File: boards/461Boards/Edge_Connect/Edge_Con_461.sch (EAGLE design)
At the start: 8 parts, among them IC1 TINY26P

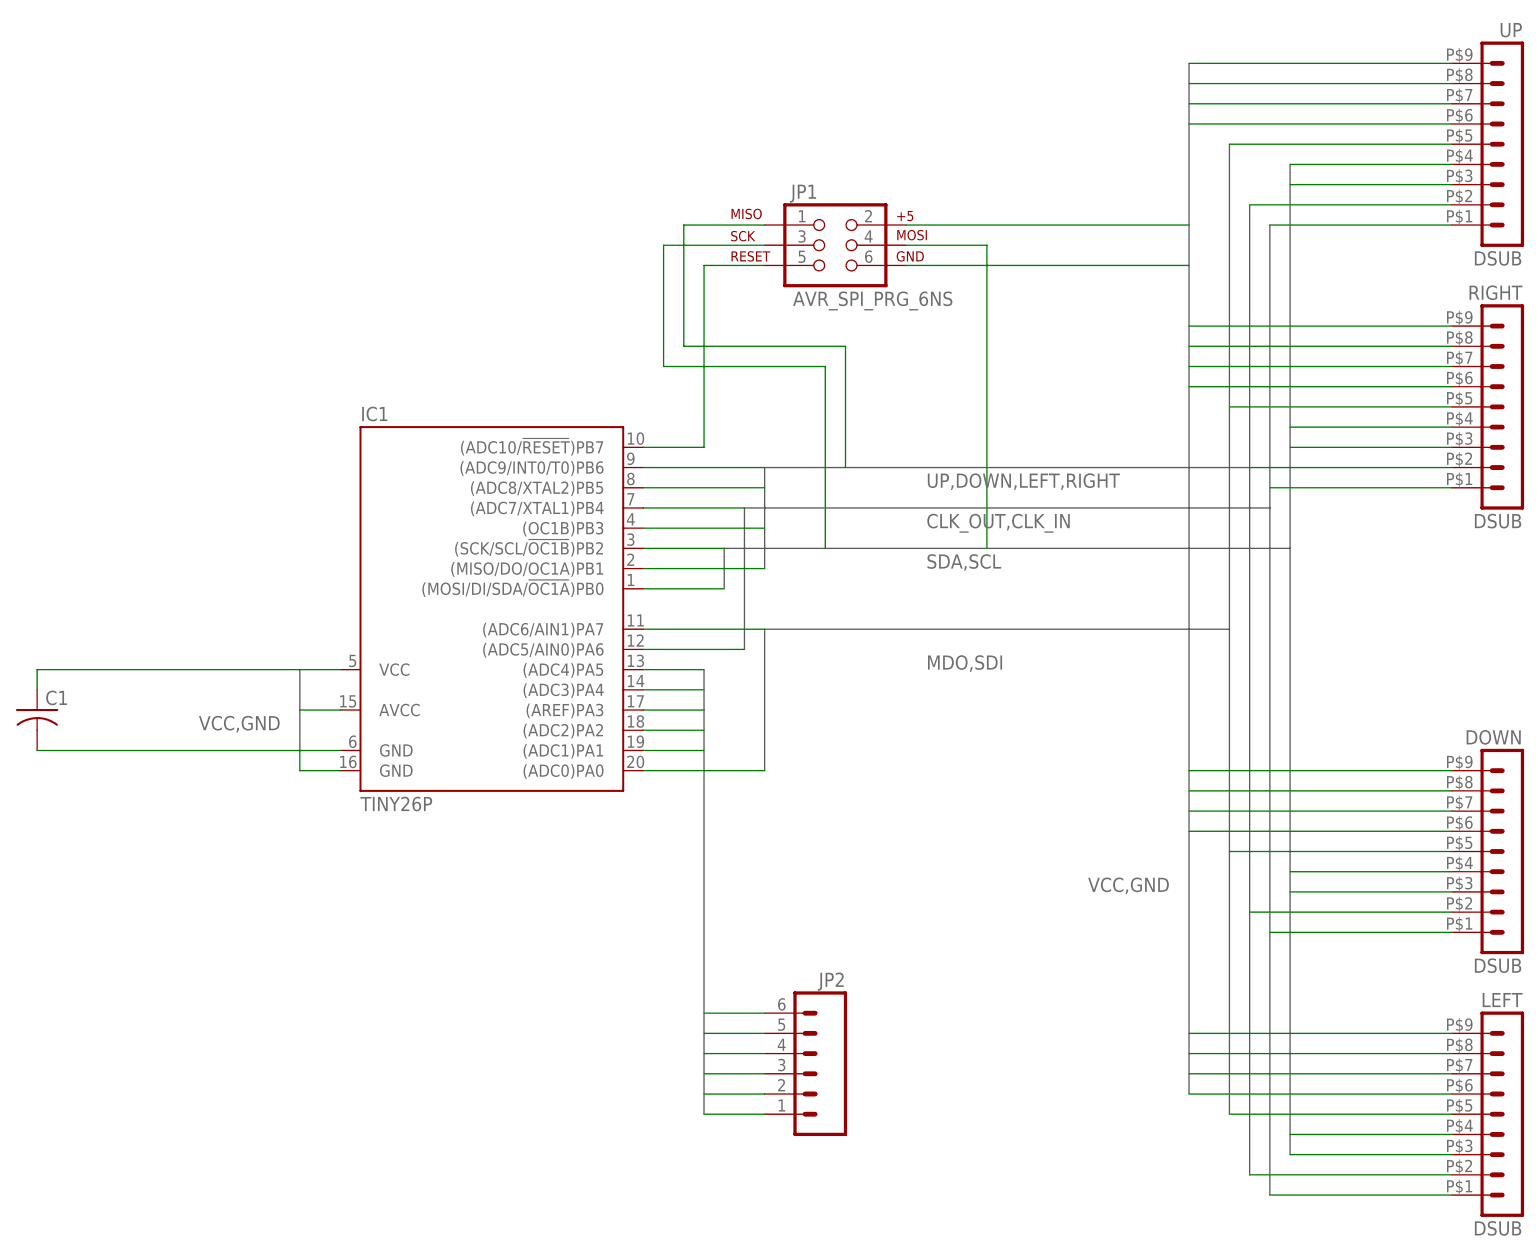
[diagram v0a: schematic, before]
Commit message: Layout in progress, one footprint needs to be added to 461_Edge Connect prior to cut.
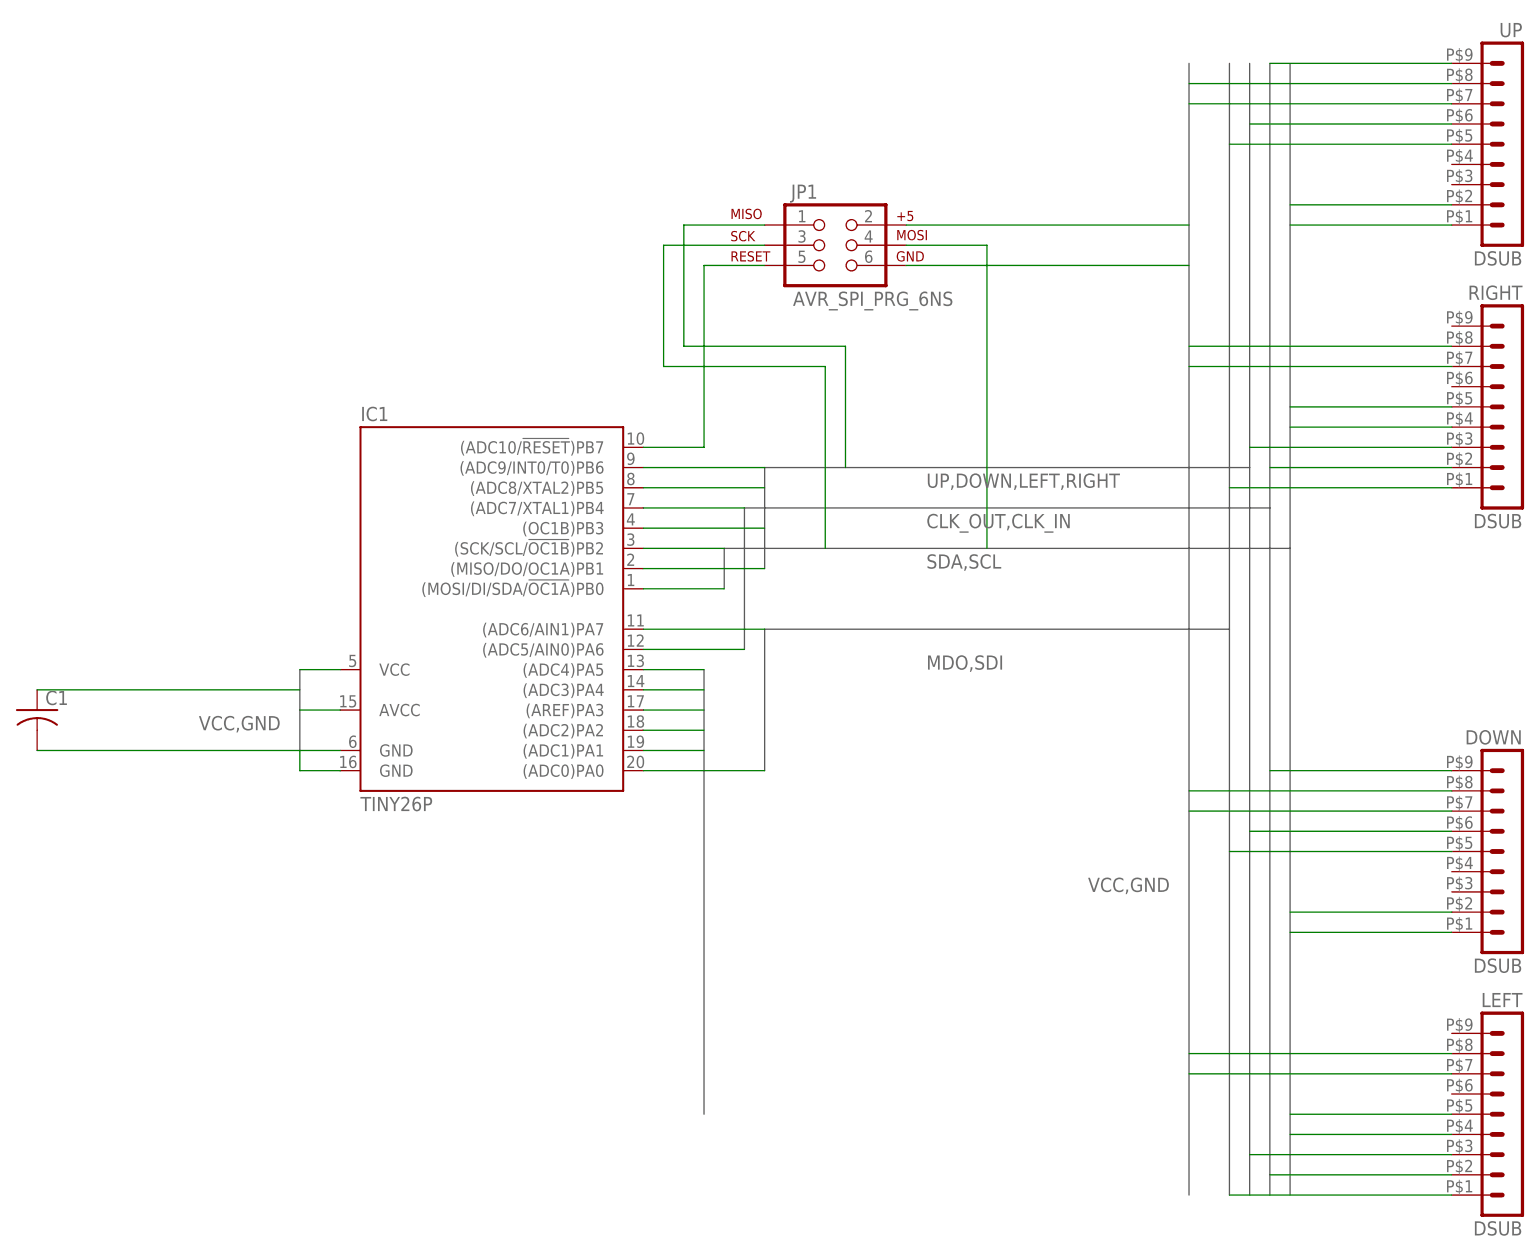
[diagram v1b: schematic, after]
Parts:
- removed JP2: (no value), SparkFun-Connectors:M06SILK_FEMALE_PTH
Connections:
- removed net 16: JP2.3
- net 13: no longer JP2.1
- net 14: no longer JP2.2
- net 17: no longer JP2.4
- net 18: no longer JP2.5
- net 19: no longer JP2.6
- net CLK_IN: now also DOWN.9, LEFT.2; no longer DOWN.1, LEFT.1
- net CLK_OUT: now also RIGHT.2, UP.9; no longer RIGHT.1, UP.1
- net DOWN: now also DOWN.6; no longer DOWN.2
- net GND: no longer DOWN.8, LEFT.8, RIGHT.8, UP.8
- net LEFT: now also LEFT.3; no longer LEFT.2
- net MDO: now also RIGHT.1; no longer RIGHT.5
- net RIGHT: now also RIGHT.3; no longer RIGHT.2
- net SCL: now also DOWN.2, LEFT.5, RIGHT.5, UP.2; no longer DOWN.4, LEFT.4, RIGHT.4, UP.4
- net SDA: now also DOWN.1, LEFT.4, RIGHT.4, UP.1; no longer DOWN.3, LEFT.3, RIGHT.3, UP.3
- net SDI: now also LEFT.1; no longer LEFT.5
- net UP: now also UP.6; no longer UP.2
- net VCC: now also DOWN.8, LEFT.8, RIGHT.8, UP.8; no longer DOWN.6, DOWN.9, LEFT.6, LEFT.9, RIGHT.6, RIGHT.9, UP.6, UP.9

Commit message: Edge Connect Layout Complete V1.0, 3 Jumper Function Select, 2 LED spaces available, Push Button Reset.
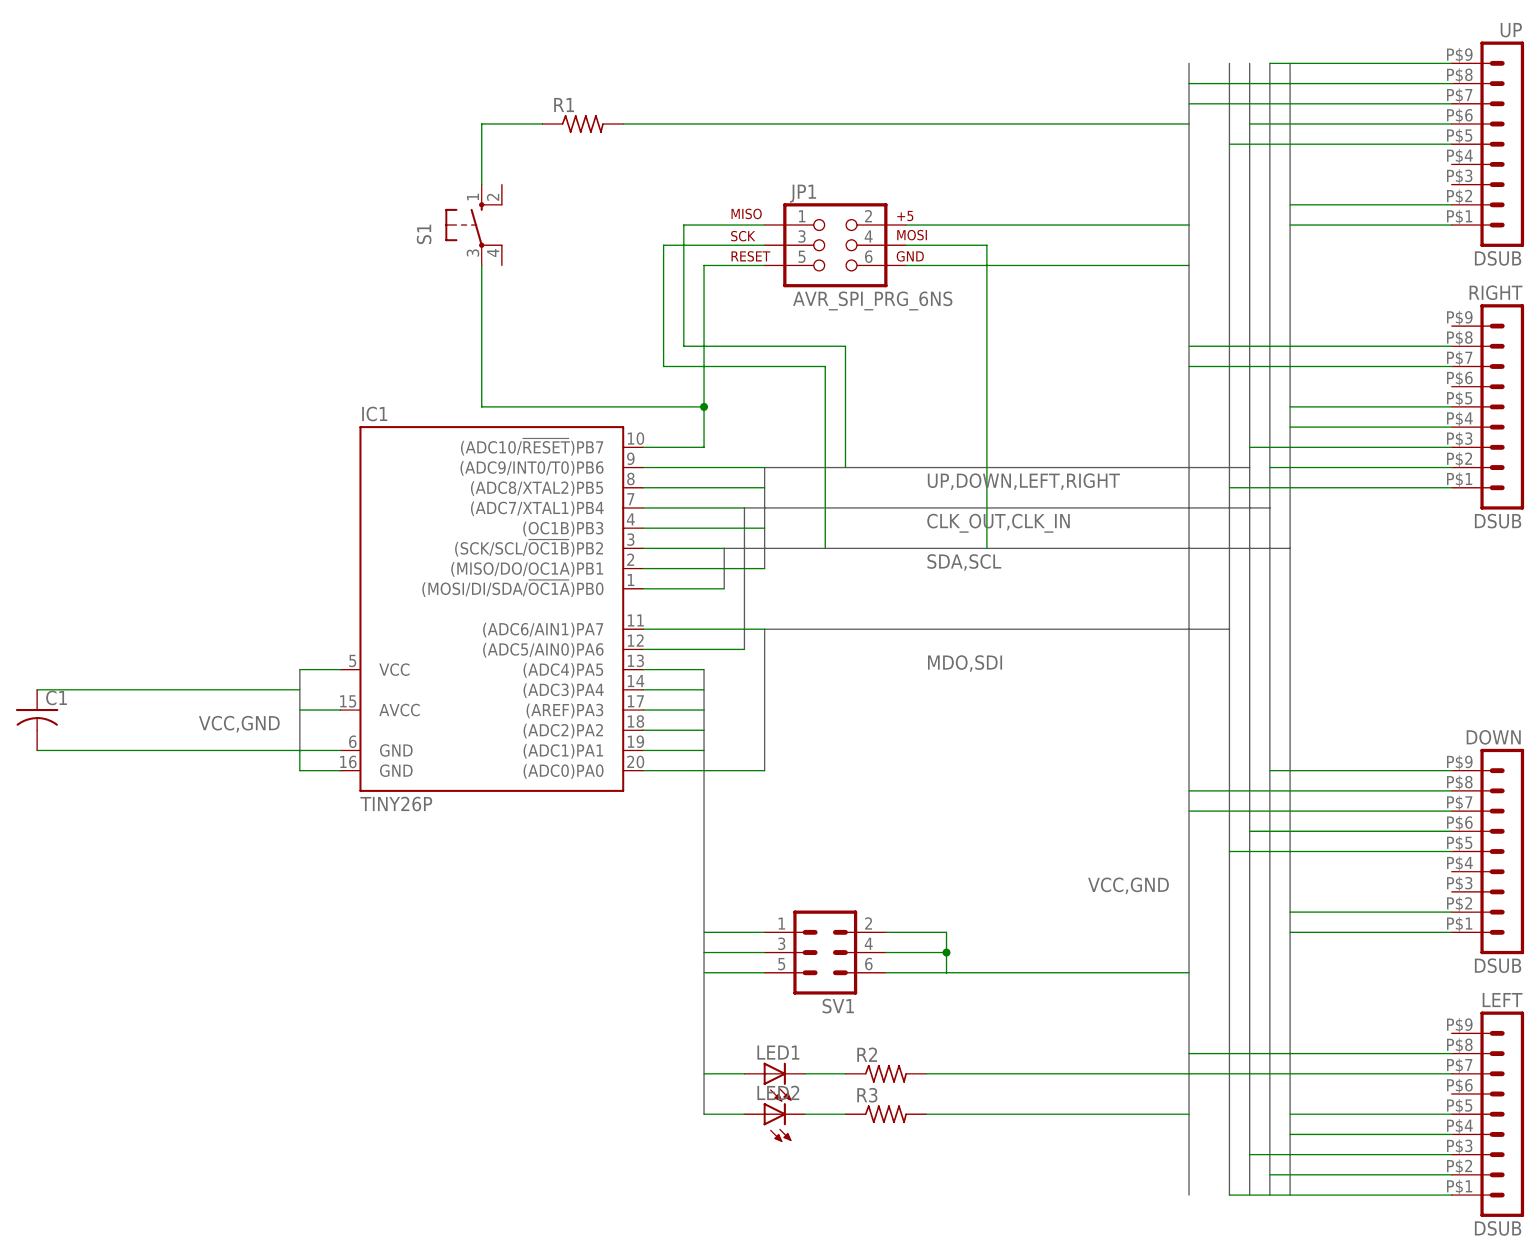
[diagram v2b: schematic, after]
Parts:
- added LED1, LED2: (no value), led:LED3MM
- added R1, R2, R3: (no value), rcl:R-US_0204/5
- added S1: (no value), switch-omron:10-XX
- added SV1: (no value), con-lstb:MA03-2
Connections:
- new net N$2: R1.1, S1.S
- new net N$3: LED1.C, R2.1
- new net N$4: LED2.C, R3.1
- net 13: now also LED1.A
- net 14: now also LED2.A
- net 17: now also SV1.5
- net 18: now also SV1.3
- net 19: now also SV1.1
- net GND: now also R1.2, R2.2, R3.2, SV1.2, SV1.4, SV1.6
- net N$1: now also S1.P
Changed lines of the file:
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@@
 <part name="JP1" library="SparkFun-Connectors" deviceset="AVR_SPI_PRG_6" device="NS"/>
 <part name="C1" library="rcl" deviceset="C-US" device="025-025X050"/>
+<part name="SV1" library="con-lstb" deviceset="MA03-2" device=""/>
+<part name="S1" library="switch-omron" deviceset="10-XX" device=""/>
+<part name="R1" library="rcl" deviceset="R-US_" device="0204/5"/>
+<part name="R2" library="rcl" deviceset="R-US_" device="0204/5"/>
+<part name="R3" library="rcl" deviceset="R-US_" device="0204/5"/>
+<part name="LED1" library="led" deviceset="LED" device="3MM"/>
+<part name="LED2" library="led" deviceset="LED" device="3MM"/>
 </parts>
 <sheets>
@@
 <instance part="JP1" gate="G$1" x="-33.02" y="53.34"/>
 <instance part="C1" gate="G$1" x="-132.08" y="-5.08"/>
+<instance part="SV1" gate="1" x="-33.02" y="-35.56" rot="R180"/>
+<instance part="S1" gate="1" x="-76.2" y="55.88"/>
+<instance part="R1" gate="G$1" x="-63.5" y="68.58"/>
+<instance part="R2" gate="G$1" x="-25.4" y="-50.8"/>
+<instance part="R3" gate="G$1" x="-25.4" y="-55.88"/>
+<instance part="LED1" gate="G$1" x="-40.64" y="-50.8" rot="R90"/>
+<instance part="LED2" gate="G$1" x="-40.64" y="-55.88" rot="R90"/>
 </instances>
 <busses>
@@
 <wire x1="-132.08" y1="-10.16" x2="-99.06" y2="-10.16" width="0.1524" layer="91"/>
 </segment>
+<segment>
+<pinref part="SV1" gate="1" pin="2"/>
+<wire x1="-25.4" y1="-33.02" x2="-17.78" y2="-33.02" width="0.1524" layer="91"/>
+<pinref part="SV1" gate="1" pin="6"/>
+<wire x1="-17.78" y1="-33.02" x2="-17.78" y2="-35.56" width="0.1524" layer="91"/>
+<wire x1="-17.78" y1="-35.56" x2="-17.78" y2="-38.1" width="0.1524" layer="91"/>
+<wire x1="-17.78" y1="-38.1" x2="-25.4" y2="-38.1" width="0.1524" layer="91"/>
+<pinref part="SV1" gate="1" pin="4"/>
+<wire x1="-25.4" y1="-35.56" x2="-17.78" y2="-35.56" width="0.1524" layer="91"/>
+<junction x="-17.78" y="-35.56"/>
+<wire x1="12.7" y1="-38.1" x2="-17.78" y2="-38.1" width="0.1524" layer="91"/>
+</segment>
+<segment>
+<pinref part="R1" gate="G$1" pin="2"/>
+<wire x1="-58.42" y1="68.58" x2="12.7" y2="68.58" width="0.1524" layer="91"/>
+</segment>
+<segment>
+<pinref part="R2" gate="G$1" pin="2"/>
+<wire x1="-20.32" y1="-50.8" x2="12.7" y2="-50.8" width="0.1524" layer="91"/>
+</segment>
+<segment>
+<pinref part="R3" gate="G$1" pin="2"/>
+<wire x1="-20.32" y1="-55.88" x2="12.7" y2="-55.88" width="0.1524" layer="91"/>
+</segment>
 </net>
 <net name="13" class="0">
@@
 <wire x1="-55.88" y1="0" x2="-48.26" y2="0" width="0.1524" layer="91"/>
 </segment>
+<segment>
+<pinref part="LED1" gate="G$1" pin="A"/>
+<wire x1="-48.26" y1="-50.8" x2="-43.18" y2="-50.8" width="0.1524" layer="91"/>
+</segment>
 </net>
 <net name="14" class="0">
@@
 <wire x1="-55.88" y1="-2.54" x2="-48.26" y2="-2.54" width="0.1524" layer="91"/>
 </segment>
+<segment>
+<pinref part="LED2" gate="G$1" pin="A"/>
+<wire x1="-48.26" y1="-55.88" x2="-43.18" y2="-55.88" width="0.1524" layer="91"/>
+</segment>
 </net>
 <net name="17" class="0">
@@
 <wire x1="-55.88" y1="-5.08" x2="-48.26" y2="-5.08" width="0.1524" layer="91"/>
 </segment>
+<segment>
+<pinref part="SV1" gate="1" pin="5"/>
+<wire x1="-40.64" y1="-38.1" x2="-48.26" y2="-38.1" width="0.1524" layer="91"/>
+</segment>
 </net>
 <net name="18" class="0">
@@
 <wire x1="-55.88" y1="-7.62" x2="-48.26" y2="-7.62" width="0.1524" layer="91"/>
 </segment>
+<segment>
+<pinref part="SV1" gate="1" pin="3"/>
+<wire x1="-40.64" y1="-35.56" x2="-48.26" y2="-35.56" width="0.1524" layer="91"/>
+</segment>
 </net>
 <net name="19" class="0">
@@
 <wire x1="-55.88" y1="-10.16" x2="-48.26" y2="-10.16" width="0.1524" layer="91"/>
 </segment>
+<segment>
+<pinref part="SV1" gate="1" pin="1"/>
+<wire x1="-40.64" y1="-33.02" x2="-48.26" y2="-33.02" width="0.1524" layer="91"/>
+</segment>
 </net>
 <net name="N$1" class="0">
@@
 <pinref part="IC1" gate="G$1" pin="(ADC10/!RESET!)PB7"/>
 <wire x1="-55.88" y1="27.94" x2="-48.26" y2="27.94" width="0.1524" layer="91"/>
-<wire x1="-48.26" y1="27.94" x2="-48.26" y2="50.8" width="0.1524" layer="91"/>
+<wire x1="-48.26" y1="27.94" x2="-48.26" y2="33.02" width="0.1524" layer="91"/>
 <pinref part="JP1" gate="G$1" pin="5"/>
+<wire x1="-48.26" y1="33.02" x2="-48.26" y2="50.8" width="0.1524" layer="91"/>
 <wire x1="-48.26" y1="50.8" x2="-40.64" y2="50.8" width="0.1524" layer="91"/>
-</segment>
-</net>
+<pinref part="S1" gate="1" pin="P"/>
+<wire x1="-48.26" y1="33.02" x2="-76.2" y2="33.02" width="0.1524" layer="91"/>
+<wire x1="-76.2" y1="33.02" x2="-76.2" y2="50.8" width="0.1524" layer="91"/>
+<junction x="-48.26" y="33.02"/>
+</segment>
+</net>
+<net name="N$2" class="0">
+<segment>
+<pinref part="S1" gate="1" pin="S"/>
+<wire x1="-76.2" y1="60.96" x2="-76.2" y2="68.58" width="0.1524" layer="91"/>
+<pinref part="R1" gate="G$1" pin="1"/>
+<wire x1="-76.2" y1="68.58" x2="-68.58" y2="68.58" width="0.1524" layer="91"/>
+</segment>
+</net>
+<net name="N$3" class="0">
+<segment>
+<pinref part="LED1" gate="G$1" pin="C"/>
+<pinref part="R2" gate="G$1" pin="1"/>
+<wire x1="-35.56" y1="-50.8" x2="-30.48" y2="-50.8" width="0.1524" layer="91"/>
+</segment>
+</net>
+<net name="N$4" class="0">
+<segment>
+<pinref part="LED2" gate="G$1" pin="C"/>
+<pinref part="R3" gate="G$1" pin="1"/>
+<wire x1="-35.56" y1="-55.88" x2="-30.48" y2="-55.88" width="0.1524" layer="91"/>
+</segment>
+</net>
